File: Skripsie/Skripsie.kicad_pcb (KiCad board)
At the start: 2 copper layers, 200 x 165 mm, 290 parts, among them J1 STM32F4_Discovery, J10 LED_R_TEST, J11 3V3, J12 UART_TEST, J13 USB_B, J2 LCD_TEST, J3 BTN_C_TEST, J4 LED_C_TEST, J5 LED_SER_TEST, J6 BTN_SER_TEST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

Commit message: Further corrections
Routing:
- net LCD_DB5: track 50.5 -> 52.4 mm
- net LCD_DB4: track 43.3 -> 44.4 mm
- net LCD_E: track 103.2 -> 102.5 mm
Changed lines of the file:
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@@
     (thickness 1.6)
     (drawings 4)
-    (tracks 2894)
+    (tracks 2896)
     (zones 0)
     (modules 290)
@@
   )
   (setup
-    (last_trace_width 0.3048)
+    (last_trace_width 1.27)
     (user_trace_width 0.3048)
     (user_trace_width 0.508)
@@
   (segment (start 132.715 31.115) (end 132.715 31.115) (width 1.27) (layer F.Cu) (net 142))
   (via (at 132.715 31.115) (size 1.6002) (drill 0.8001) (layers F.Cu B.Cu) (net 142))
-  (segment (start 133.35 29.21) (end 132.715 29.845) (width 1.27) (layer B.Cu) (net 142))
-  (segment (start 151.765 29.21) (end 133.35 29.21) (width 1.27) (layer B.Cu) (net 142))
   (segment (start 153.035 30.48) (end 151.765 29.21) (width 1.27) (layer B.Cu) (net 142))
   (segment (start 153.035 34.925) (end 153.035 30.48) (width 1.27) (layer B.Cu) (net 142))
@@
   (segment (start 167.005 56.515) (end 168.275 55.245) (width 1.27) (layer B.Cu) (net 142))
   (segment (start 155.575 53.975) (end 155.575 55.88) (width 1.27) (layer B.Cu) (net 142))
-  (segment (start 132.715 29.845) (end 132.715 31.115) (width 1.27) (layer B.Cu) (net 142))
   (segment (start 155.575 55.88) (end 156.21 56.515) (width 1.27) (layer B.Cu) (net 142))
   (segment (start 168.275 55.245) (end 168.275 52.705) (width 1.27) (layer B.Cu) (net 142))
@@
   (segment (start 171.14521 42.87521) (end 171.14521 39.342172) (width 1.27) (layer B.Cu) (net 142))
   (segment (start 153.67 35.56) (end 153.035 34.925) (width 1.27) (layer B.Cu) (net 142))
+  (segment (start 139.065 29.21) (end 137.16 31.115) (width 1.27) (layer B.Cu) (net 142))
+  (segment (start 151.765 29.21) (end 139.065 29.21) (width 1.27) (layer B.Cu) (net 142))
+  (segment (start 137.16 31.115) (end 132.715 31.115) (width 1.27) (layer B.Cu) (net 142))
   (segment (start 153.035 52.772919) (end 153.035 53.975) (width 1.27) (layer B.Cu) (net 143))
   (segment (start 151.697081 51.435) (end 153.035 52.772919) (width 1.27) (layer B.Cu) (net 143))
@@
   (segment (start 158.115 53.975) (end 158.115 52.07) (width 1.27) (layer B.Cu) (net 145))
   (segment (start 158.115 52.07) (end 161.925 48.26) (width 1.27) (layer B.Cu) (net 145))
-  (segment (start 161.925 45.787919) (end 157.412081 41.275) (width 1.27) (layer B.Cu) (net 145))
-  (segment (start 161.925 46.99) (end 161.925 45.787919) (width 1.27) (layer B.Cu) (net 145))
   (via (at 151.220975 41.275) (size 1.6002) (drill 0.8001) (layers F.Cu B.Cu) (net 145))
-  (segment (start 157.412081 41.275) (end 151.220975 41.275) (width 1.27) (layer B.Cu) (net 145))
   (segment (start 135.255 40.005) (end 136.525 41.275) (width 1.27) (layer F.Cu) (net 145))
   (segment (start 136.525 41.275) (end 151.220975 41.275) (width 1.27) (layer F.Cu) (net 145))
   (segment (start 135.255 40.005) (end 135.255 35.56) (width 1.27) (layer F.Cu) (net 145))
+  (segment (start 161.925 43.815) (end 161.925 46.99) (width 1.27) (layer B.Cu) (net 145))
+  (segment (start 161.29 43.18) (end 161.925 43.815) (width 1.27) (layer B.Cu) (net 145))
+  (segment (start 159.317081 43.18) (end 161.29 43.18) (width 1.27) (layer B.Cu) (net 145))
+  (segment (start 151.220975 41.275) (end 157.412081 41.275) (width 1.27) (layer B.Cu) (net 145))
+  (segment (start 157.412081 41.275) (end 159.317081 43.18) (width 1.27) (layer B.Cu) (net 145))
   (segment (start 164.465 46.99) (end 164.465 48.26) (width 1.27) (layer B.Cu) (net 146))
   (segment (start 160.655 53.975) (end 160.655 52.07) (width 1.27) (layer B.Cu) (net 146))
   (segment (start 160.655 52.07) (end 164.465 48.26) (width 1.27) (layer B.Cu) (net 146))
-  (segment (start 164.465 45.72) (end 164.465 46.99) (width 1.27) (layer B.Cu) (net 146))
   (via (at 160.655 41.275) (size 1.6002) (drill 0.8001) (layers F.Cu B.Cu) (net 146))
-  (segment (start 164.465 45.085) (end 164.465 45.72) (width 1.27) (layer B.Cu) (net 146))
-  (segment (start 160.655 41.275) (end 164.465 45.085) (width 1.27) (layer B.Cu) (net 146))
   (segment (start 159.385 40.005) (end 160.655 41.275) (width 0.635) (layer F.Cu) (net 146))
   (segment (start 151.765 40.005) (end 159.385 40.005) (width 0.635) (layer F.Cu) (net 146))
@@
   (segment (start 150.495 31.75) (end 150.495 38.735) (width 0.635) (layer F.Cu) (net 146))
   (segment (start 150.495 38.735) (end 151.765 40.005) (width 0.635) (layer F.Cu) (net 146))
+  (segment (start 163.83 41.275) (end 160.655 41.275) (width 1.27) (layer B.Cu) (net 146))
+  (segment (start 164.465 46.99) (end 164.465 41.91) (width 1.27) (layer B.Cu) (net 146))
+  (segment (start 164.465 41.91) (end 163.83 41.275) (width 1.27) (layer B.Cu) (net 146))
   (segment (start 167.005 46.99) (end 167.005 48.26) (width 1.27) (layer B.Cu) (net 147))
   (segment (start 163.195 53.975) (end 163.195 52.07) (width 1.27) (layer B.Cu) (net 147))

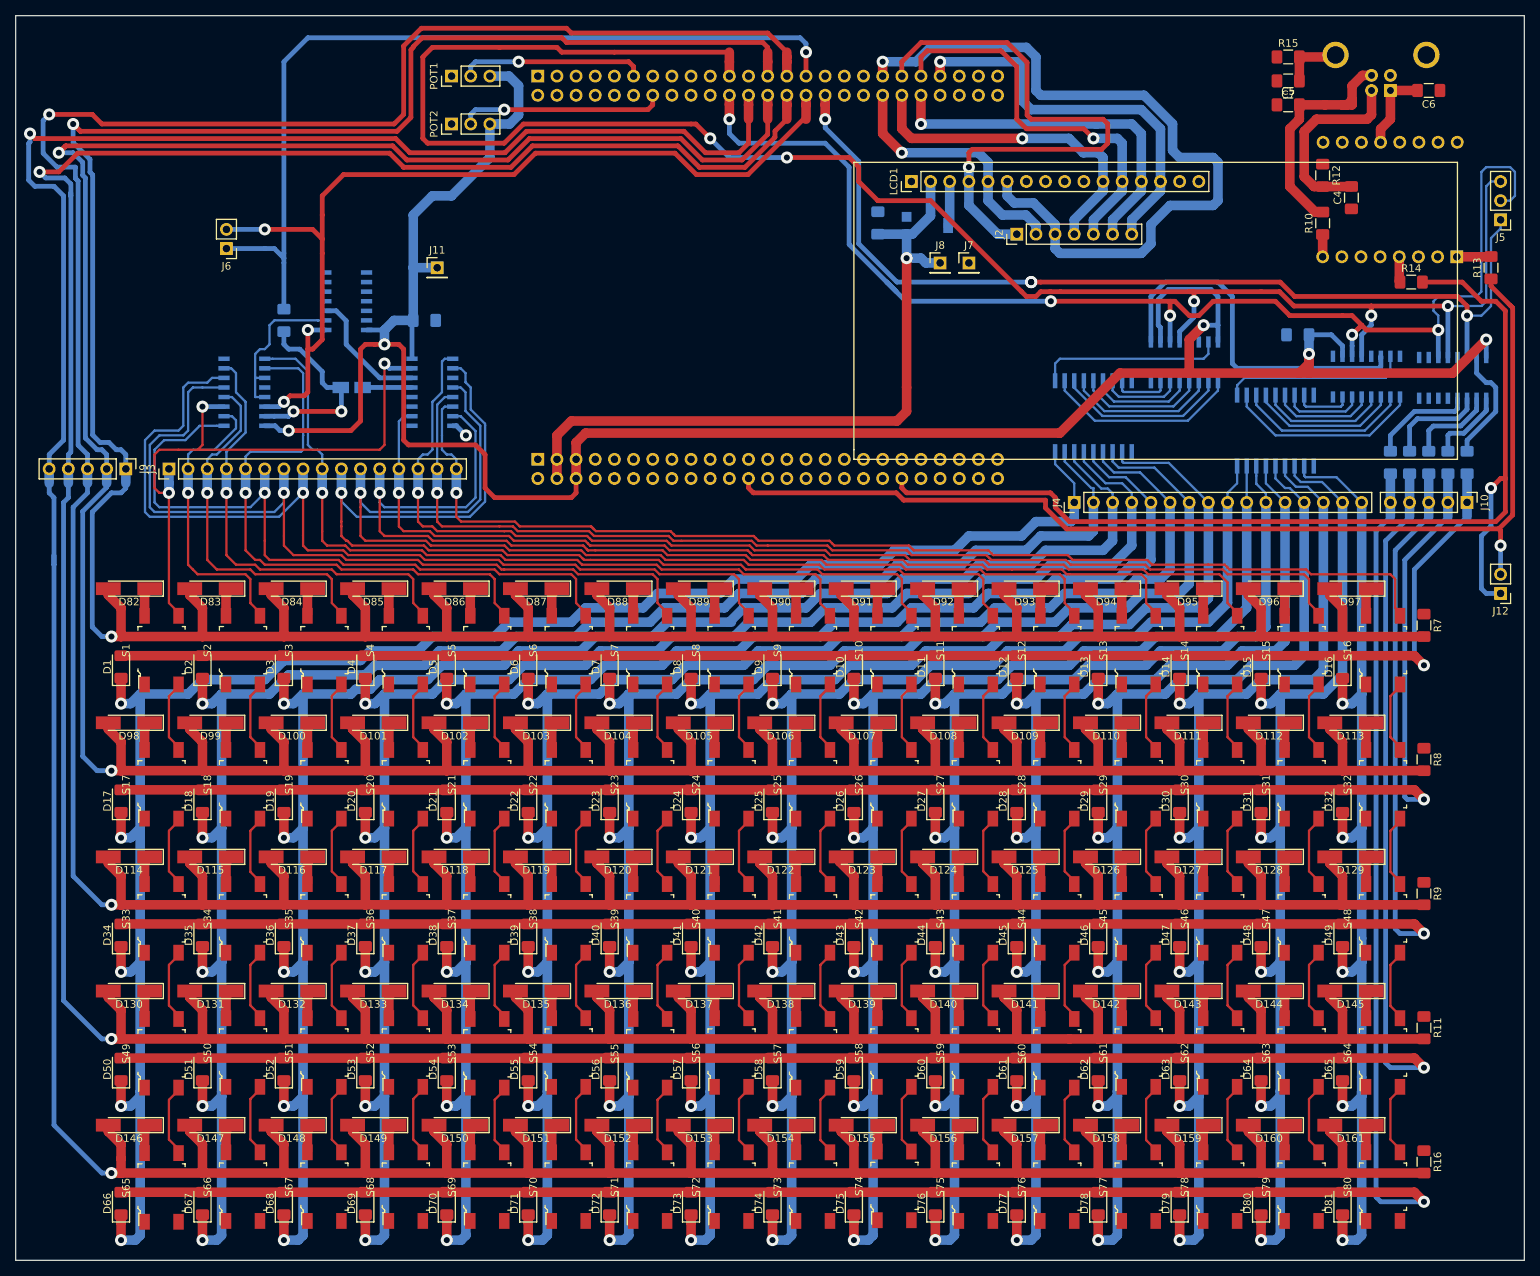
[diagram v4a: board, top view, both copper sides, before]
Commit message: Infill Added to PCB
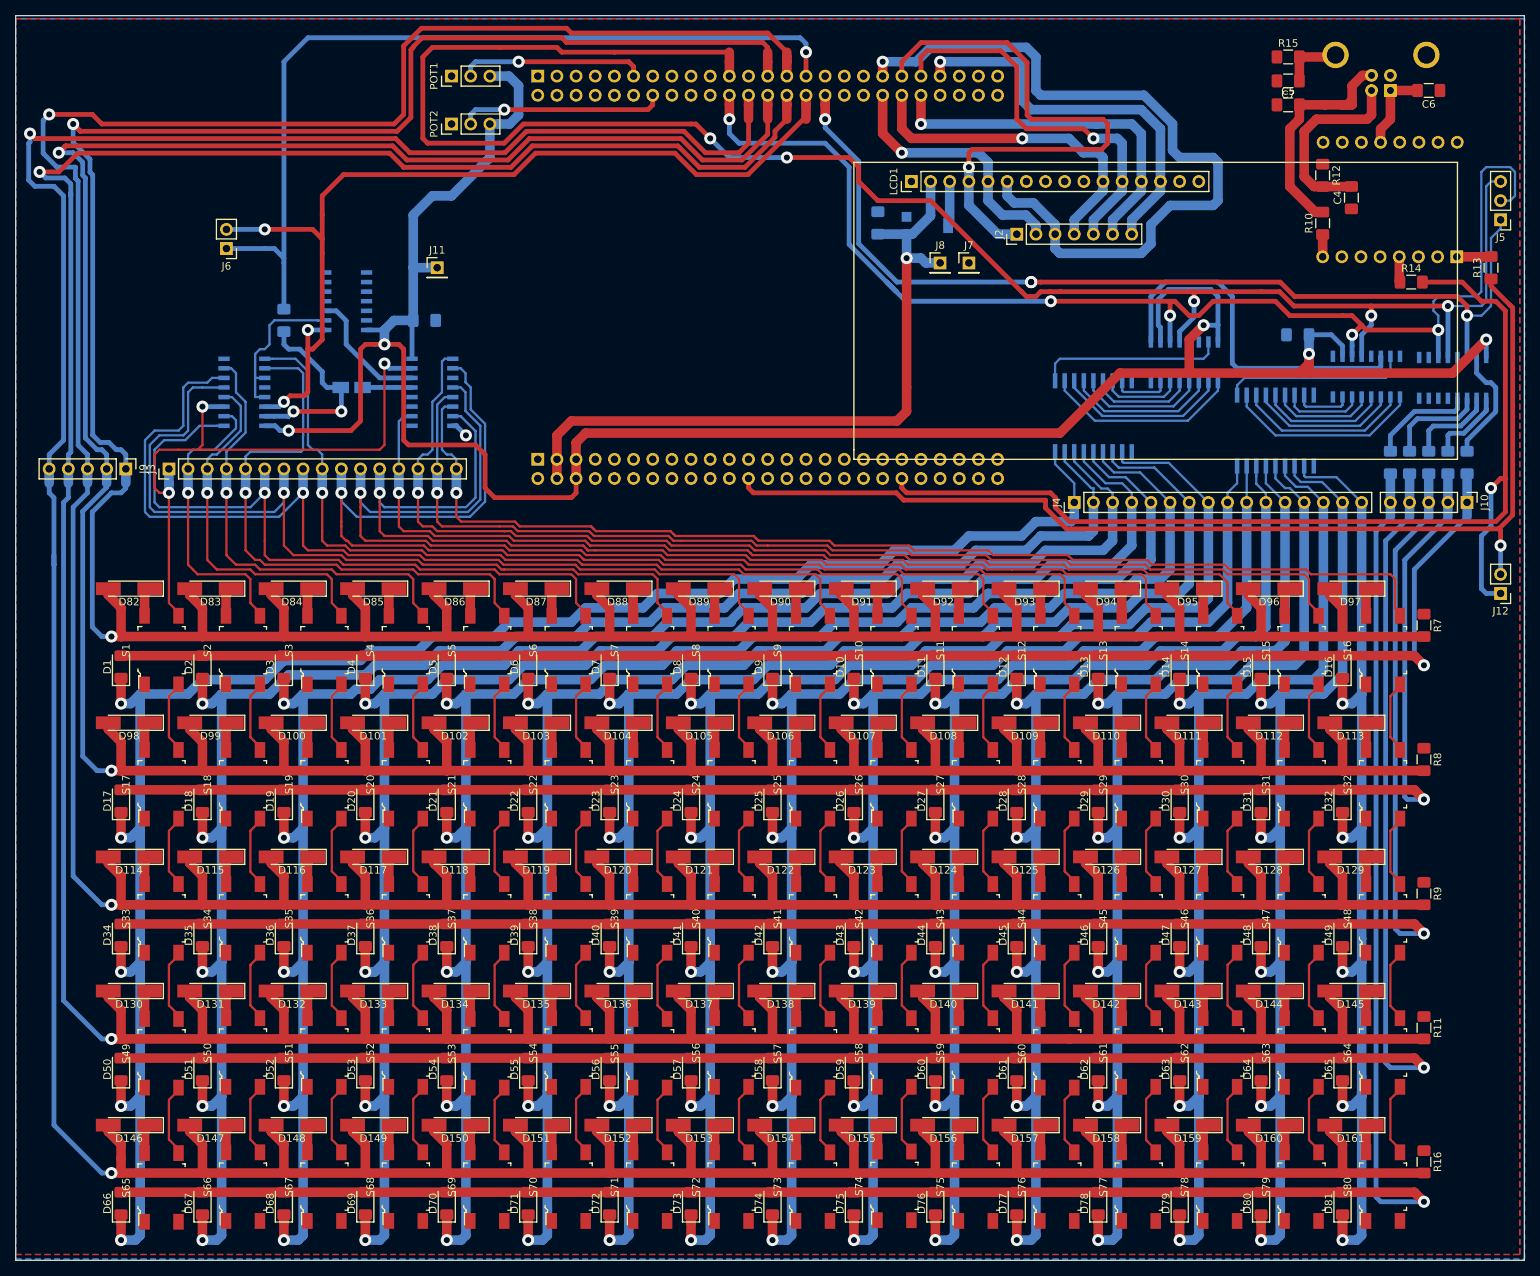
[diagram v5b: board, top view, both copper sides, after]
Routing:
- added copper zone on B.Cu, net (none)
- added copper zone on F.Cu, net (none)
- added copper zone on B.Cu, net GND
- added copper zone on F.Cu, net GND
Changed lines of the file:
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@@
   (segment (start 66.04 73.025) (end 61.595 68.58) (width 0.635) (layer B.Cu) (net 247))
   (segment (start 70.325 73.025) (end 66.04 73.025) (width 0.635) (layer B.Cu) (net 247))
+  (zone (net 1) (net_name GND) (layer B.Cu) (hatch edge 0.508)
+    (connect_pads (clearance 0.508))
+    (min_thickness 0.254)
+    (fill yes (arc_segments 32) (thermal_gap 0.508) (thermal_bridge_width 0.508))
+    (polygon
+      (pts
+        (xy 17.78 25.4) (xy 17.78 189.865) (xy 217.805 189.865) (xy 217.805 25.4)
+      )
+    )
+  )
+  (zone (net 0) (net_name "") (layer B.Cu) (hatch edge 0.508)
+    (connect_pads (clearance 0.508))
+    (min_thickness 0.254)
+    (fill yes (arc_segments 16) (thermal_gap 0.508) (thermal_bridge_width 0.508))
+    (polygon
+      (pts
+        (xy 17.78 25.4) (xy 17.78 189.865) (xy 217.805 189.865) (xy 217.805 25.4)
+      )
+    )
+  )
+  (zone (net 1) (net_name GND) (layer F.Cu) (hatch edge 0.508)
+    (connect_pads (clearance 0.508))
+    (min_thickness 0.254)
+    (fill yes (arc_segments 16) (thermal_gap 0.508) (thermal_bridge_width 0.508))
+    (polygon
+      (pts
+        (xy 17.78 25.4) (xy 17.78 189.23) (xy 217.17 189.23) (xy 217.17 25.4)
+      )
+    )
+  )
+  (zone (net 0) (net_name "") (layer F.Cu) (hatch edge 0.508)
+    (connect_pads (clearance 0.508))
+    (min_thickness 0.254)
+    (fill yes (arc_segments 16) (thermal_gap 0.508) (thermal_bridge_width 0.508))
+    (polygon
+      (pts
+        (xy 17.78 25.4) (xy 17.78 189.23) (xy 217.17 189.23) (xy 217.17 25.4)
+      )
+    )
+  )
 )

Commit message: Gerber files added along with text and a symbol
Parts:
- added G***: LOGO, pieter:gor_sml, F.Cu at (31.8, 62.9)
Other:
- board text added: "Skripsie Drum Machine Pieter Goos (19231466) Under Dr L. Visagie Rev. B - 08/03/2019"
